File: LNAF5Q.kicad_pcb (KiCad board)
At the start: 4 copper layers, 11.7 x 8.7 mm, 25 parts, among them P1 SMA-KIT-1.5MF, U1 SWITCH, U2 SWITCH, U3 LNA, U4 SAW

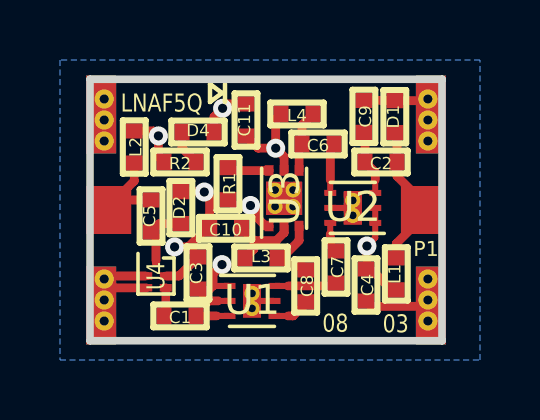
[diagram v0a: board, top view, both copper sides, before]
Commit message: correct U4 track clearance
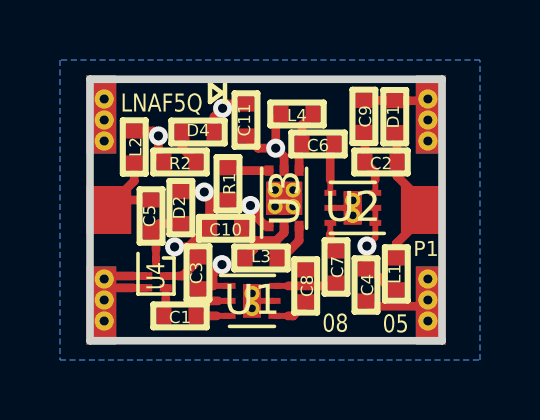
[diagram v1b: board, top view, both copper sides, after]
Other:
- board text added: "05"
- board text removed: "03"

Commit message: renumber capacitor reference designators
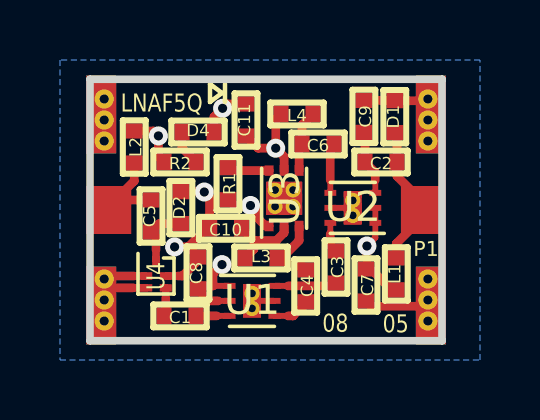
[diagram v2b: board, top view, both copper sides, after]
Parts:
- renumbered C7 to C3, C8 to C4, C4 to C7, C3 to C8

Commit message: optimize part selection for 915 MHz
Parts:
- C1, C2, C3, C4, C5, C6, C7, C8: value 100pF -> 47pF
- C9: value 1 pF -> 1pF
- L1, L2, L3, L4: value 39nH -> 100nH
